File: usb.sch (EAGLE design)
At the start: 9 parts, among them J1 UJ31-CH-3-SMT-TR

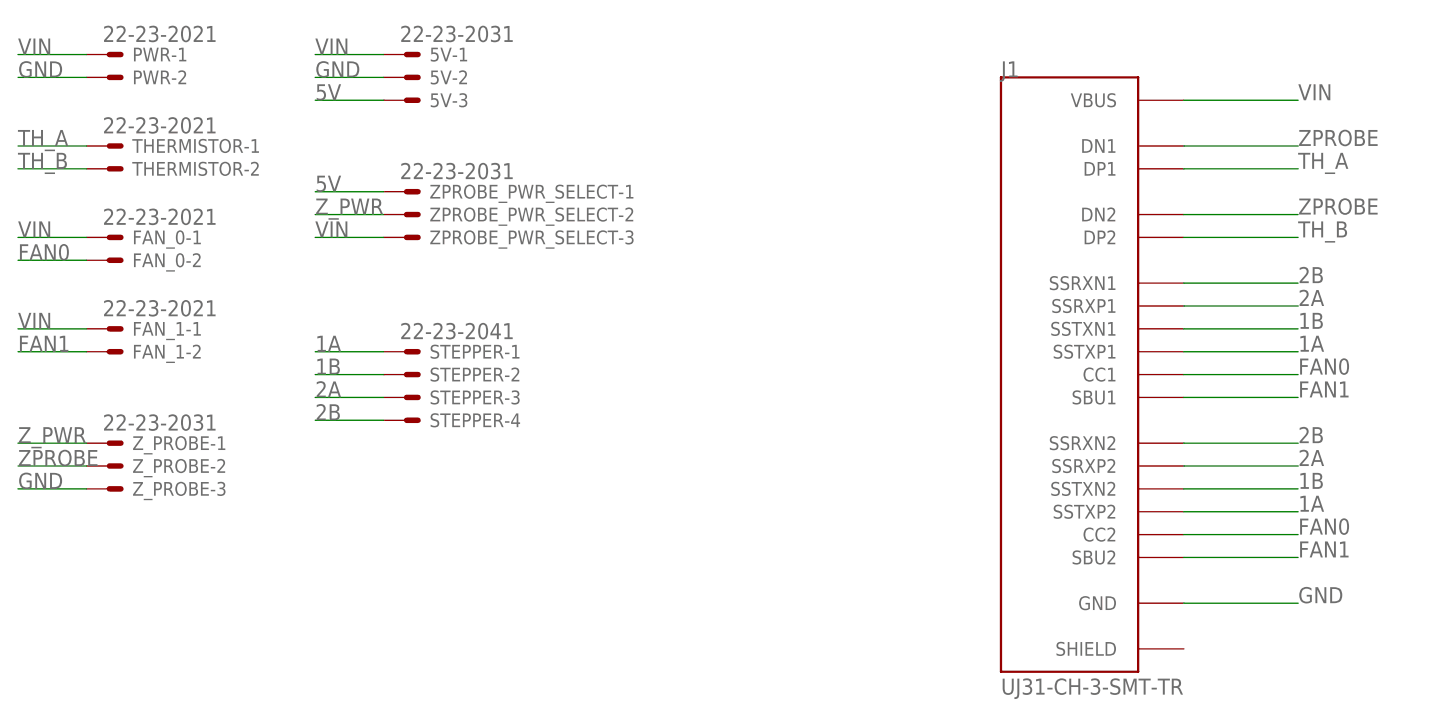
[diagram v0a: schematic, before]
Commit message: Changed to vertical plug
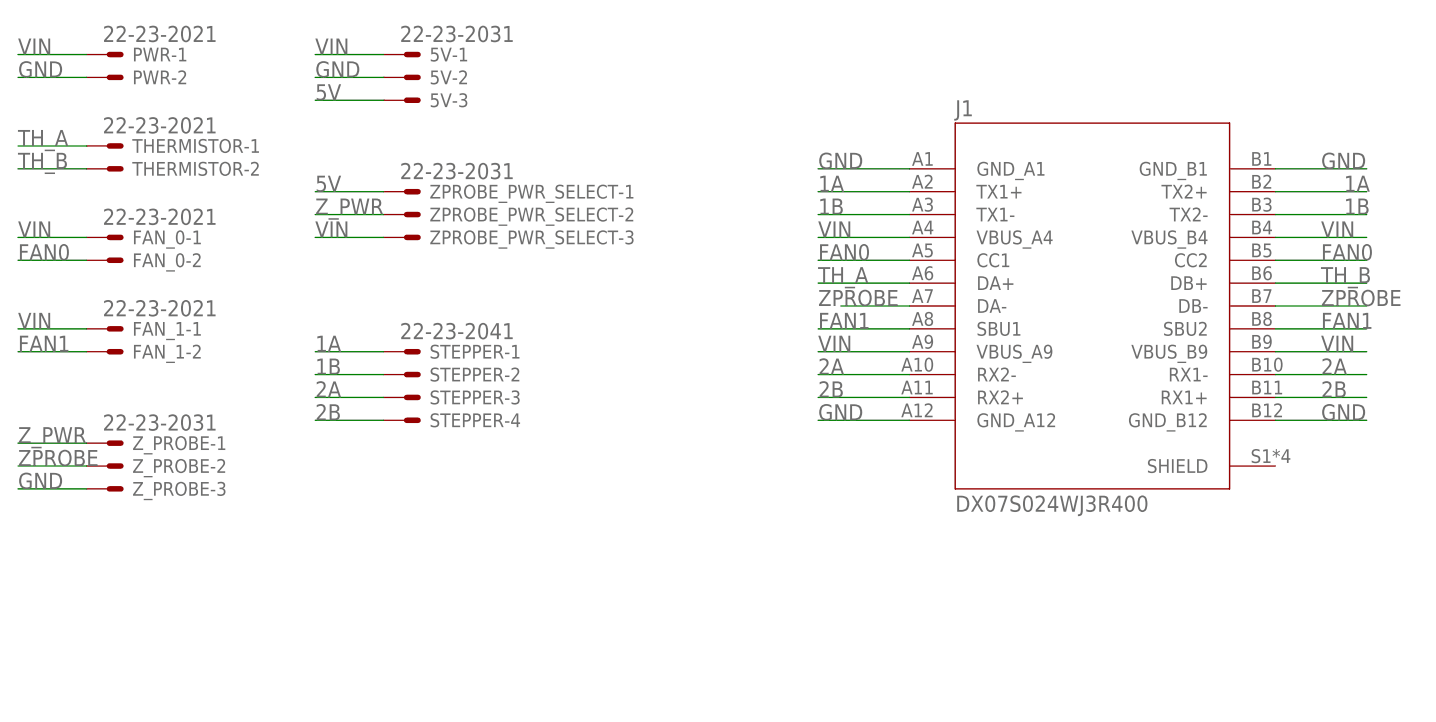
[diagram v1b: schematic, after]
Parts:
- J1: value UJ31-CH-3-SMT-TR -> DX07S024WJ3R400; device UJ31-CH-3-SMT-TR:UJ31-CH-3-SMT-TR -> DX07S024WJ3R400:DX07S024WJ3R400
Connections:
- net 1A: now also J1.TX1+, J1.TX2+; no longer J1.SSTXP1, J1.SSTXP2
- net 1B: now also J1.TX1-, J1.TX2-; no longer J1.SSTXN1, J1.SSTXN2
- net 2A: now also J1.RX1-, J1.RX2-; no longer J1.SSRXP1, J1.SSRXP2
- net 2B: now also J1.RX1+, J1.RX2+; no longer J1.SSRXN1, J1.SSRXN2
- net GND: now also J1.GND_A1, J1.GND_A12, J1.GND_B1, J1.GND_B12; no longer J1.GND
- net TH_A: now also J1.DA+; no longer J1.DP1
- net TH_B: now also J1.DB+; no longer J1.DP2
- net VIN: now also J1.VBUS_A4, J1.VBUS_A9, J1.VBUS_B4, J1.VBUS_B9; no longer J1.VBUS
- net ZPROBE: now also J1.DA-, J1.DB-; no longer J1.DN1, J1.DN2
